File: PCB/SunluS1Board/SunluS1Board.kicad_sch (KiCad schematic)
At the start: 2 parts, among them U1 STM32C011F4Px

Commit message: start base schematic
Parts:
- added C1, C2: 100nF, symbol Device:C
- added D1: LED, symbol Device:LED
- added M1: Fan, symbol Motor:Fan
- added Q1, Q2: AO3400A, Package_TO_SOT_SMD:SOT-23, symbol Transistor_FET:AO3400A
- added R2, R6: 100, symbol Device:R
- added R3, R5: 100k, symbol Device:R
- added R4: 470, symbol Device:R
- added SW1, SW2: CS1213AGF260, easyeda2kicad:SW-SMD_L3.9-W3.0-P4.45, symbol easyeda2kicad:TS-1088-AR02016
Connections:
- net +24V: now reaches R1.1
- net +24V: now also M1.1 (+)
- net at R1.2: now also Q1.3 (D)
- net B1: now reaches U1.11 (PA4)
- net B1: now also C2.1, SW1.2
- net B2: now reaches U1.12 (PA5)
- net B2: now also C1.1, SW2.2
- net MISO: now reaches U1.13 (PA6)
- net MOSI: now reaches U1.14 (PA7)
- net airNTC: now reaches U1.16 (PA9/PA11)
- net heatNTC: now reaches U1.17 (PA10/PA12)
- net SWDIO: now reaches U1.18 (PA13)
- net SWCLK: now reaches U1.19 (PA14)
- net SCK: now reaches U1.20 (PB6)
- net +3.3V: now reaches U1.4 (VDD)
- net GND: now reaches U1.5 (VSS)
- net GND: now also C1.2, C2.2, Q1.2 (S), Q2.2 (S), R3.1, R4.1, R5.1, SW1.1, SW2.1
- net NRST: now reaches U1.6 (PF2)
- net Heater: now reaches U1.7 (PA0)
- net Heater: now also R2.2
- net Fan: now reaches U1.8 (PA1)
- net Fan: now also R6.2
- net Led: now reaches U1.9 (PA2)
- net Led: now also D1.2 (A)
- new net: Q1.1 (G), R2.1, R3.2
- new net: D1.1 (K), R4.2
- new net: M1.2 (-), Q2.3 (D)
- new net: Q2.1 (G), R5.2, R6.1
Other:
- moved on the sheet: R1

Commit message: ntc
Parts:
- added R7, R8: 100k, symbol Device:R
- added TH1: 100k, symbol Device:Thermistor_NTC
- added TH2: Thermistor_NTC, symbol Device:Thermistor_NTC
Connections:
- net +3.3V: now also R7.1, R8.1
- net GND: now also TH1.2, TH2.2
- net airNTC: now also R8.2, TH2.1
- net heatNTC: now also R7.2, TH1.1

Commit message: display
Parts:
- added J1: Conn_01x14, symbol Connector_Generic:Conn_01x14
- added Q3: AO3400A, Package_TO_SOT_SMD:SOT-23, symbol Transistor_FET:AO3400A
- added R10: 100, symbol Device:R
- added R9: 100k, symbol Device:R
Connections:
- net +3.3V: now also J1.10 (Pin_10), J1.11 (Pin_11), J1.4 (Pin_4)
- net GND: now also J1.13 (Pin_13), J1.2 (Pin_2), J1.5 (Pin_5), Q3.2 (S), R9.1
- net MOSI: now also J1.8 (Pin_8)
- net SCK: now also J1.9 (Pin_9)
- net CS: now reaches U1.1 (PB7)
- net CS: now also J1.12 (Pin_12)
- net A0: now reaches U1.10 (PA3)
- net A0: now also J1.7 (Pin_7)
- net BL: now reaches U1.15 (PA8)
- net BL: now also R10.2
- net RET: now reaches U1.2 (PC14)
- net RET: now also J1.6 (Pin_6)
- net MISO: no longer names the net of U1.13 (PA6)
- new net: Q3.1 (G), R10.1, R9.2
- new net: J1.3 (Pin_3), Q3.3 (D)
- no-connect marks 0 -> 3

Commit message: finish schematic
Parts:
- removed M1: Fan, symbol Motor:Fan
- removed R1: Heater, OptoDevice:R_LDR_4.9x4.2mm_P2.54mm_Vertical, symbol Device:Heater
- added F1: Fuse, Fuse:Fuse_1206_3216Metric, symbol Device:Fuse
- added J2: aNTC, symbol Connector_Generic:Conn_01x02
- added J3: hNTC, symbol Connector_Generic:Conn_01x02
- added J4: Fan, Connector_JST:JST_XH_S2B-XH-A-1_1x02_P2.50mm_Horizontal, symbol Connector_Generic:Conn_01x02
- added J5: HT, Connector_JST:JST_XH_S2B-XH-A-1_1x02_P2.50mm_Horizontal, symbol Connector_Generic:Conn_01x02
- added J6: Power, Connector_JST:JST_XH_S2B-XH-A-1_1x02_P2.50mm_Horizontal, symbol Connector_Generic:Conn_01x02
- added U2: AP7381-33SA-7, Package_TO_SOT_SMD:SOT-23, symbol Regulator_Linear:AP7381-33SA-7
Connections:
- net +24V: now also F1.2, J4.1 (Pin_1), J5.1 (Pin_1), U2.1 (VI)
- net +3.3V: now also U2.2 (VO)
- net GND: now also J2.2 (Pin_2), J3.2 (Pin_2), J6.2 (Pin_2), U2.3 (GND)
- net airNTC: now also J2.1 (Pin_1)
- net heatNTC: now also J3.1 (Pin_1)
- net hCon: now reaches Q1.3 (D)
- net hCon: now also J5.2 (Pin_2)
- net fCon: now reaches Q2.3 (D)
- net fCon: now also J4.2 (Pin_2)
- new net: F1.1, J6.1 (Pin_1)
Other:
- moved on the sheet: R7, R8, TH1, TH2

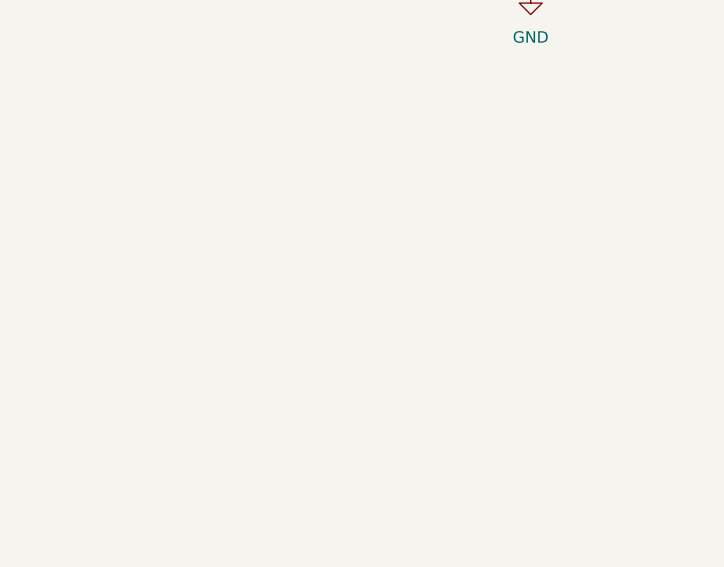
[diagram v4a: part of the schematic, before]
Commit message: add swd header
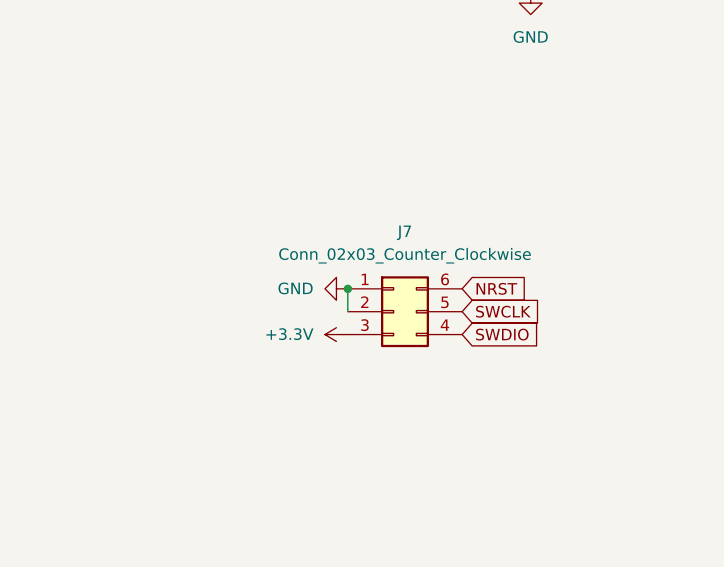
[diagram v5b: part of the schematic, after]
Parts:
- added J7: Conn_02x03_Counter_Clockwise, Connector_PinSocket_2.54mm:PinSocket_2x03_P2.54mm_Vertical_SMD, symbol Connector_Generic:Conn_02x03_Counter_Clockwise
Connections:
- net +3.3V: now also J7.3 (Pin_3)
- net GND: now also J7.1 (Pin_1), J7.2 (Pin_2)
- net NRST: now also J7.6 (Pin_6)
- net SWCLK: now also J7.5 (Pin_5)
- net SWDIO: now also J7.4 (Pin_4)

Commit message: refine schematic
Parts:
- added C10, C4, C6, C8: 10uF, symbol Device:C
- added C11, C12, C3, C5, C7, C9: 100nF, symbol Device:C
- added R1, R11: 100, symbol Device:R
- added R12: 10k, symbol Device:R
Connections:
- net +24V: now also C10.1, C5.1, C6.1, C9.1
- net +3.3V: now also C3.1, C4.1, C7.1, C8.1, R12.1
- net GND: now also C10.2, C11.2, C12.2, C3.2, C4.2, C5.2, C6.2, C7.2, C8.2, C9.2
- net NRST: now also R12.2
- net airNTC: now also C12.1, R1.1; no longer J2.1 (Pin_1)
- net heatNTC: now also C11.1, R11.1; no longer J3.1 (Pin_1)
- new net: J2.1 (Pin_1), R1.2
- new net: J3.1 (Pin_1), R11.2

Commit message: more decaps
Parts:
- added C13: 10uF, symbol Device:C
- added C14: 100nF, symbol Device:C
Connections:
- net +3.3V: now also C13.1, C14.1
- net GND: now also C13.2, C14.2

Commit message: custom footprint
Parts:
- J1: footprint (none) -> Extra:STP0177A-128160
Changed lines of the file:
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@@
 			)
 		)
-		(property "Footprint" ""
+		(property "Footprint" "Extra:STP0177A-128160"
 			(at 257.81 40.64 0)
 			(effects
